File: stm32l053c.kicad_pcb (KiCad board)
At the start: 2 copper layers, 20.8 x 43.7 mm, 17 parts, among them P1 SWD, P2 CONN_01X17, P3 CONN_01X17, P4 Ext Xtal, SW1 RESET, U1 STM32L053C8_LQFP48

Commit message: Solder bridges
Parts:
- R2, R3: footprint Resistors_SMD:R_0805_HandSoldering -> Resistors_SMD:R_0402
- moved P4 1.06 mm to (191.8, 85.3)
- moved R2 0.44 mm to (191.8, 89.8)
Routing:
- net VDD: track 66.7 -> 93.6 mm, vias 4 -> 5
- net Earth: track 116.3 -> 109.4 mm
- net /VLCD: track 5.58 -> 6.88 mm
- net /VDD_USB: track 13.2 -> 14.1 mm

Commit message: Extra ground
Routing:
- net Earth: track 109.4 -> 122.7 mm
- net NRST: track 50.4 -> 51.3 mm
- net OSC32_OUT: track 17.8 -> 17.0 mm
- net OSC32_IN: track 15.0 -> 14.3 mm

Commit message: LED
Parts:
- added D1: LED, LEDs:LED_0805, F.Cu at (191.8, 109.2)
- added R4: 820, Resistors_SMD:R_0805_HandSoldering, B.Cu at (191.8, 110.5)
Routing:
- net /PA5: track 6.45 -> 20.6 mm, vias 0 -> 1
- net Net-(D1-Pad2): track 0.00 -> 4.77 mm, vias 0 -> 1
- net Earth: track 122.7 -> 125.0 mm

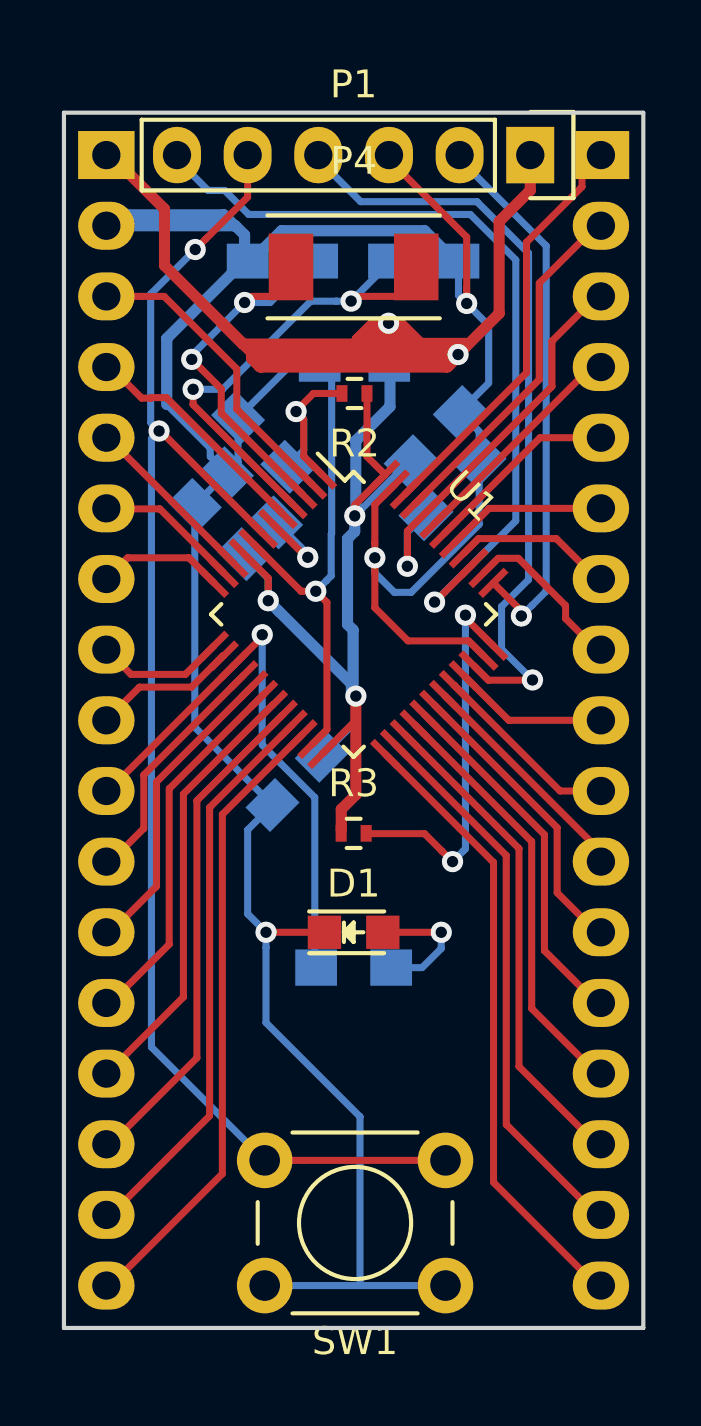
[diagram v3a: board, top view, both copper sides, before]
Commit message: Silkscreen labels
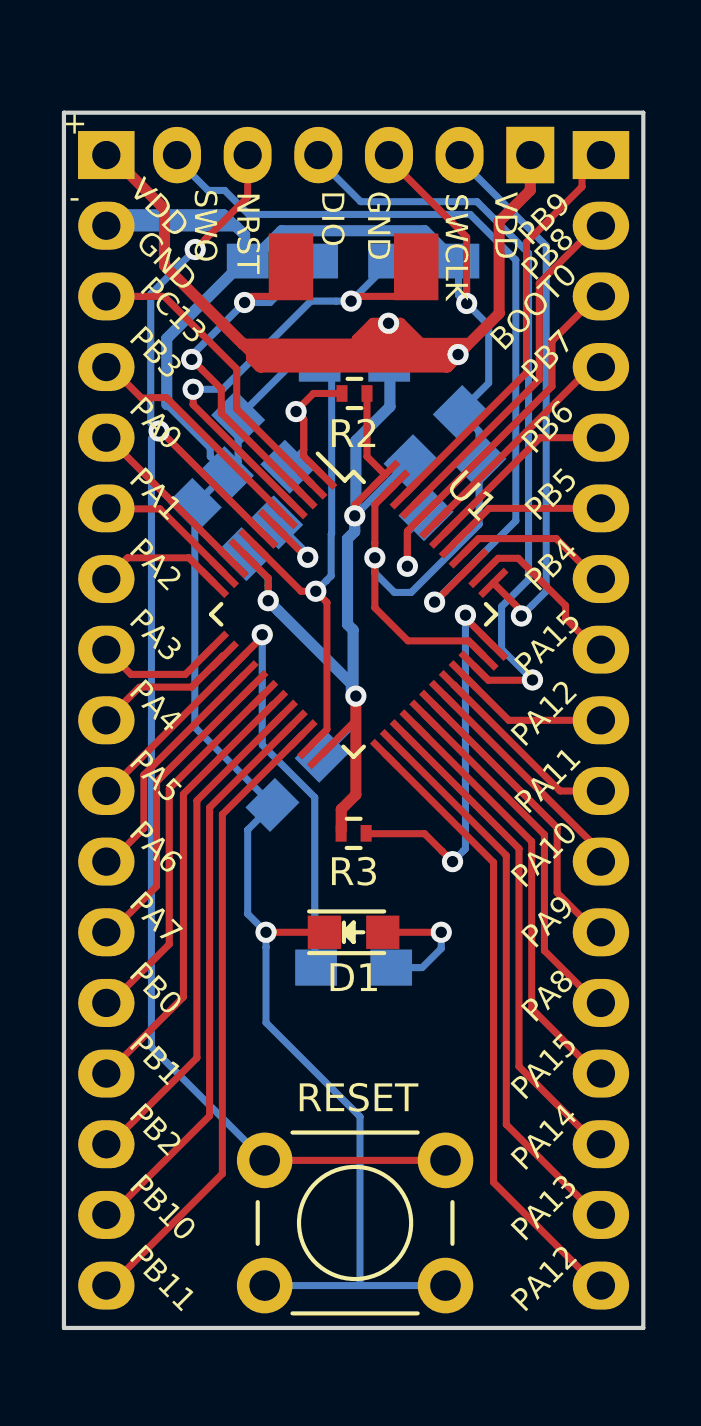
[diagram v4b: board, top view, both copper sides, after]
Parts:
- P1: footprint Pin_Headers:Pin_Header_Straight_1x06 -> Pin_Header_Straight_1x06
- P4: footprint Crystals:Crystal_SMD_0603_2Pads_obsolete -> Crystal_SMD_0603_2Pads
- renumbered SW1 to RESET
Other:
- board text added: "+"
- board text added: "-"
- board text added: "BOOT0"
- board text added: "DIO"
- board text added: "GND"
- board text added: "NRST"
- board text added: "PA0"
- board text added: "PA1"
- board text added: "PA10"
- board text added: "PA11"
- board text added: "PA12"
- board text added: "PA13"
- board text added: "PA14"
- board text added: "PA15"
- board text added: "PA2"
- board text added: "PA3"
- board text added: "PA4"
- board text added: "PA5"
- board text added: "PA6"
- board text added: "PA7"
- board text added: "PA8"
- board text added: "PA9"
- board text added: "PB0"
- board text added: "PB1"
- board text added: "PB10"
- board text added: "PB11"
- board text added: "PB2"
- board text added: "PB3"
- board text added: "PB4"
- board text added: "PB5"
- board text added: "PB6"
- board text added: "PB7"
- board text added: "PB8"
- board text added: "PB9"
- board text added: "PC13"
- board text added: "SWCLK"
- board text added: "SWO"
- board text added: "VDD"

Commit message: Logos
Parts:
- added REF**: TheApiLogo, theapi:TheApiLogoSmall, B.Cu at (192.0, 112.0)
- added REF**: TheApiLogoTiny, theapi:TheApiLogoTiny, F.Cu at (191.9, 110.5)
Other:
- board text added: "github.com/theapi/STM32L053C_breakout_board v1.0"
